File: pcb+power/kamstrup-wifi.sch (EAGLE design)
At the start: 23 parts, among them T1 BT137S-600D, T2 BT137S-600D

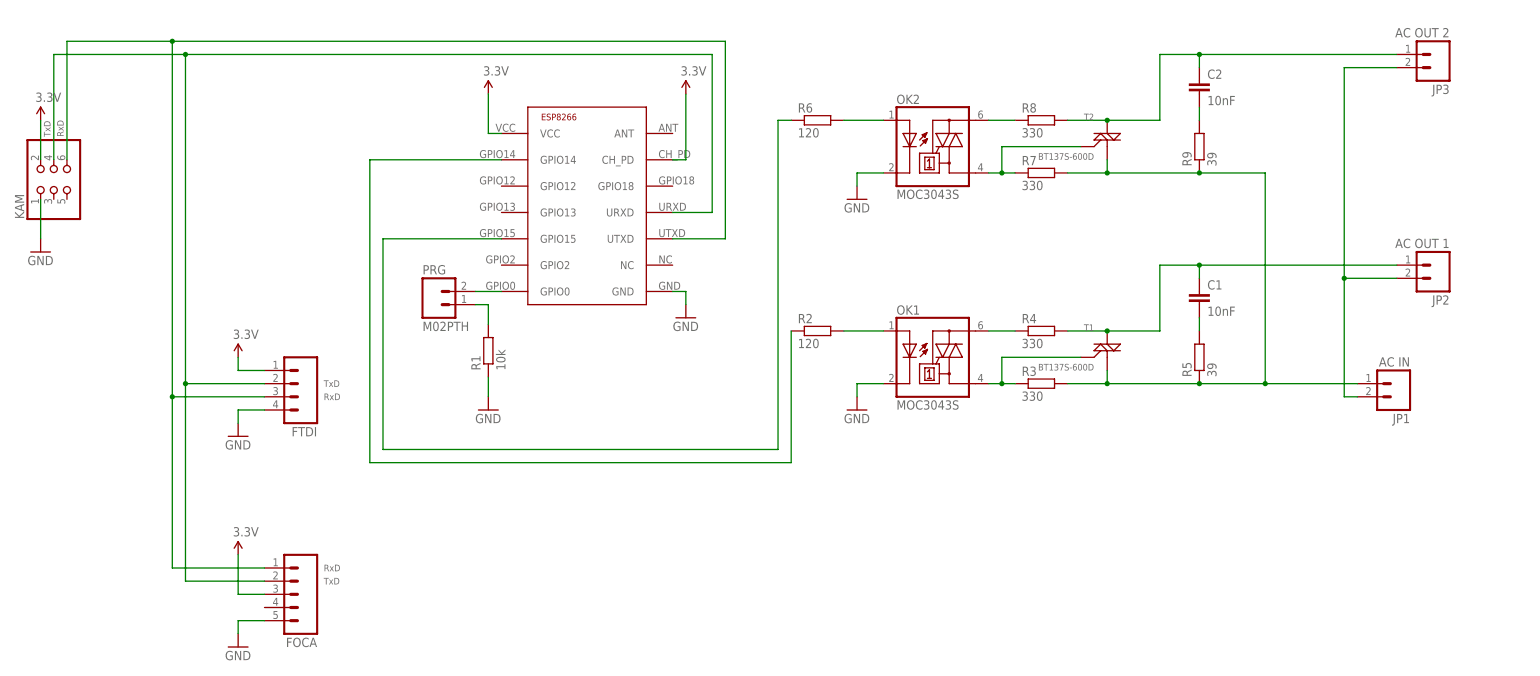
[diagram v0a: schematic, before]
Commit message: pcb v.1.1
triac sot428 + esp-07 pin layout
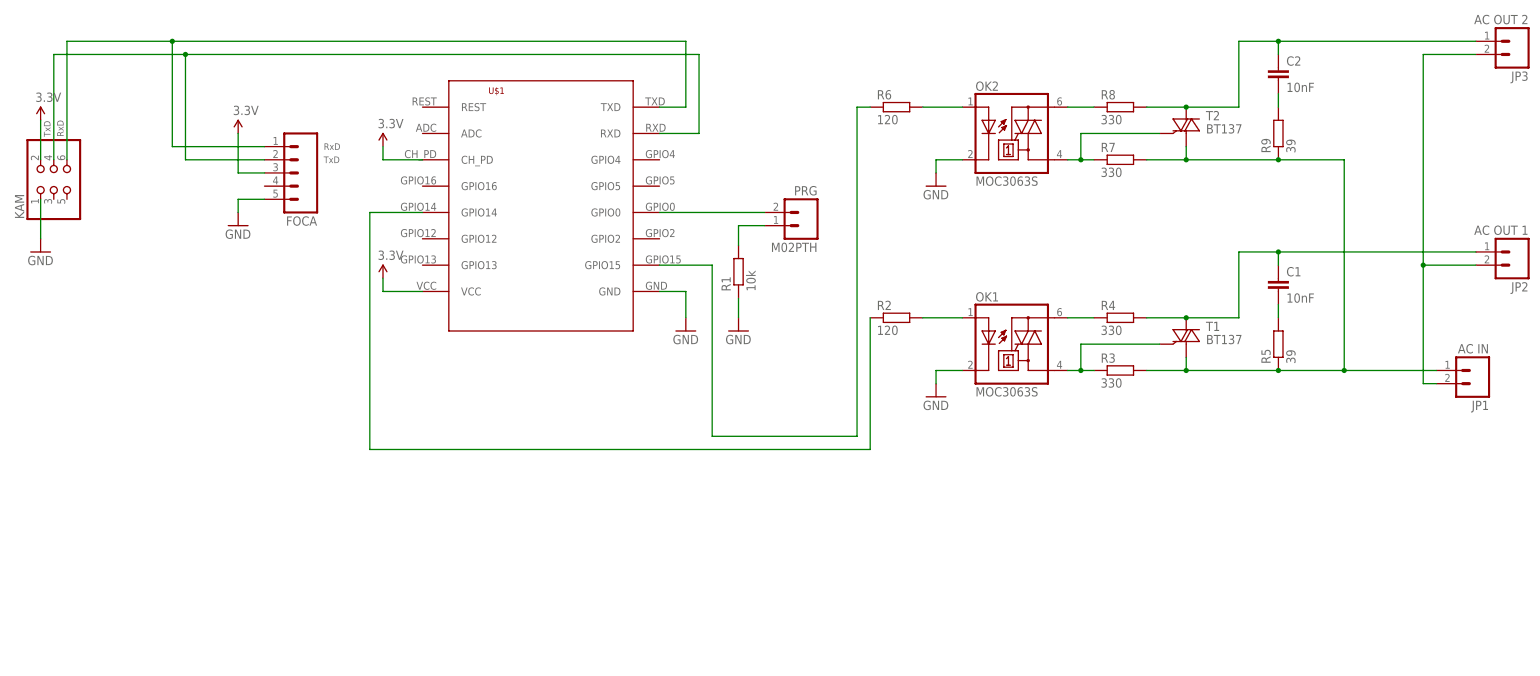
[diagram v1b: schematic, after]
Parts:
- removed FTDI: (no value), SparkFun-Connectors:M04PTH
- removed U$3: ESP8266-03, ESP8266:ESP8266-03
- added U$1: ESP8266-07, lio:ESP8266-07
- OK1, OK2: value MOC3043S -> MOC3063S
- T1, T2: value BT137S-600D -> BT137; device SparkFun (old):TRIACSMD -> Triac SOT428:BT137
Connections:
- net 3.3V: now also U$1.CH_PD, U$1.VCC; no longer FTDI.1, U$3.CH_PD, U$3.VCC
- net GND: now also U$1.GND; no longer FTDI.4, U$3.GND
- net N$1: now also U$1.TXD; no longer FTDI.3, U$3.UTXD
- net N$11: now also U$1.GPIO14; no longer U$3.GPIO14
- net N$15: now also T1.A2; no longer T1.M2
- net N$16: now also U$1.GPIO15; no longer U$3.GPIO15
- net N$2: now also U$1.RXD; no longer FTDI.2, U$3.URXD
- net N$3: now also U$1.GPIO0; no longer U$3.GPIO0
- net N$8: now also T2.A2; no longer T2.M2
- net N$9: now also T1.A1, T2.A1; no longer T1.M1, T2.M1
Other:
- moved on the sheet: C1, C2, FOCA, JP1, JP2, JP3, OK1, OK2, PRG, R1, R2, R3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
